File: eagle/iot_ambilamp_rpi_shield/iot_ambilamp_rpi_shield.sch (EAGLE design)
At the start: 15 parts, among them IC1 MCP3008, J1 RPI-GPIO, J2 SOUND DETECTOR, J3 DHT22

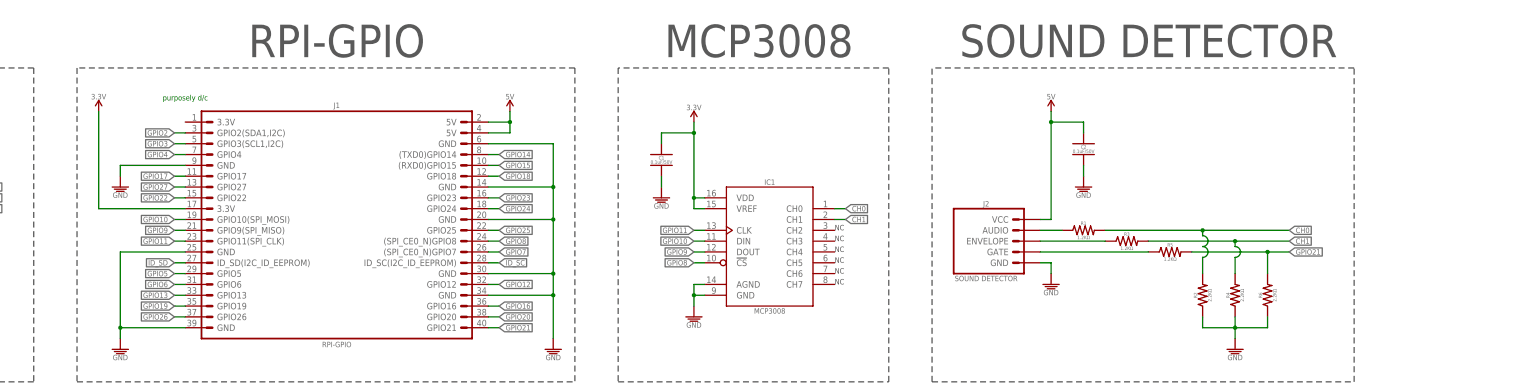
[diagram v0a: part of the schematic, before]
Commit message: Rev 3: Add Serial (Console) Cable access.  TX, RX, and GND.  Changed components to PiB library parts
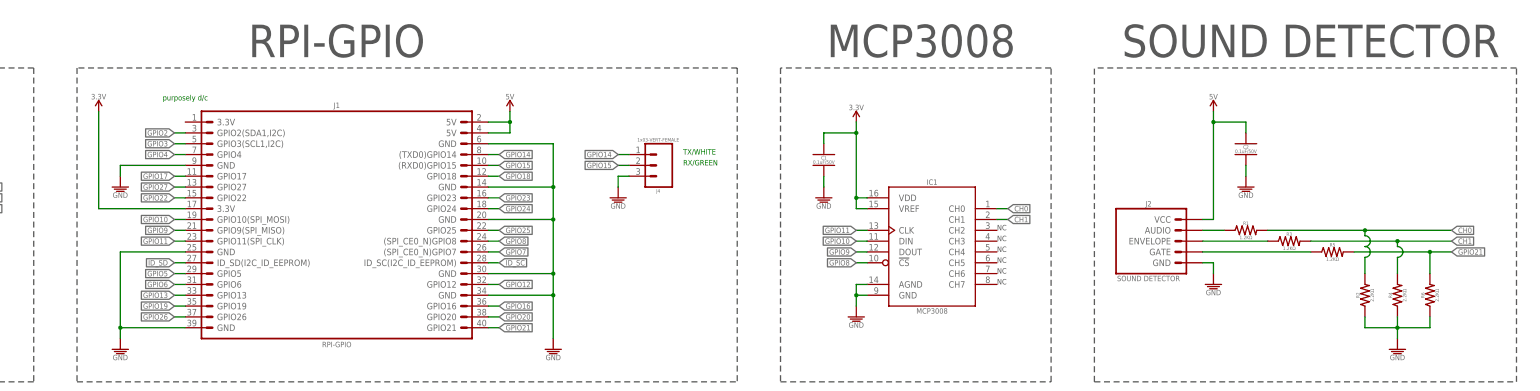
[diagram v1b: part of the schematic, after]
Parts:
- added J4: 1x03-VERT-FEMALE, PiB_connectors:1X03_VERT-FEMALE
- C1, C2, C3: device MrSwirlyEyes:CAP_CERAMIC_SMD-805_0.1UF-50V-10% -> PiB_capacitors:0.1UF_SMD-805_50V-10%
- IC1: device lib_swirly:MCP3008SO-16 -> PiB:MCP3008SO-16
- J1: device MrSwirlyEyes:RPI-GPIO_CONNECTOR -> PiB_connectors:RPI-GPIO_CONNECTOR
- J3: device lib_swirly:TEMPERATURE-SENSOR_DHT22 -> PiB:TEMPERATURE-SENSOR_DHT22
- L1: device MrSwirlyEyes:LED-5MM-PTH_RGB-CA -> PiB_leds:LED-5MM-PTH_RGB-CA
- R1, R3, R5: device MrSwirlyEyes:RESISTORSMD-0805_1/8W_1.2K_5% -> PiB_resistors:1.2KΩ_SMD-0805_1/8W-5%
- R2, R4, R6: device MrSwirlyEyes:RESISTORSMD-0805_1/8W_2.2K_5% -> PiB_resistors:2.2KΩ_SMD-0805_1/8W-5%
- R7: device MrSwirlyEyes:RESISTORSMD-0805_1/8W_10K_5% -> PiB_resistors:10KΩ_SMD-0805_1/8W-5%
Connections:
- net GND: now also J4.3
- net GPIO14: now also J4.1
- net GPIO15: now also J4.2
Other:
- note added: "RX/GREEN"
- note added: "TX/WHITE"
- moved on the sheet: C1, C2, IC1, J2, R1, R2, R3, R4, R5, R6
